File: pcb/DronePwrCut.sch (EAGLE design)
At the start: 55 parts, among them IC1 ATMega48, IC2 MIC5219-3.6YM5-TR, M1 AUIRFS8409-7P, M2 AUIRFS8409-7P, M3 AUIRFS8409-7P, M4 AUIRFS8409-7P, Q1 NF, X1 ISP

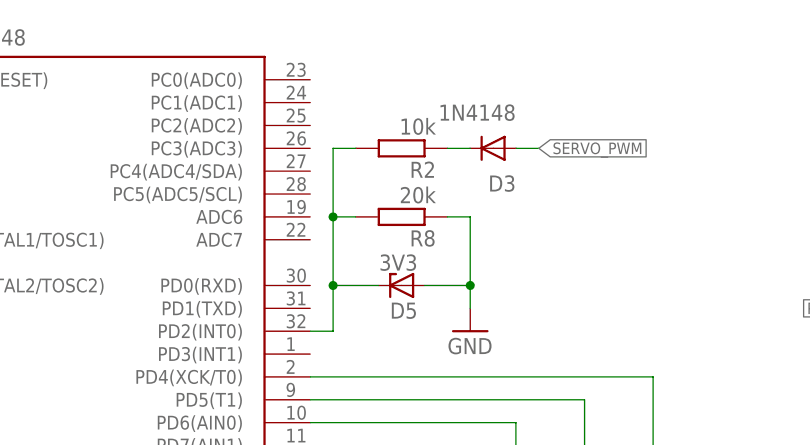
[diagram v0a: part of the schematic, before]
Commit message: Change resistor values (R2, R8) to handle low voltage (3V3) input signals correctly
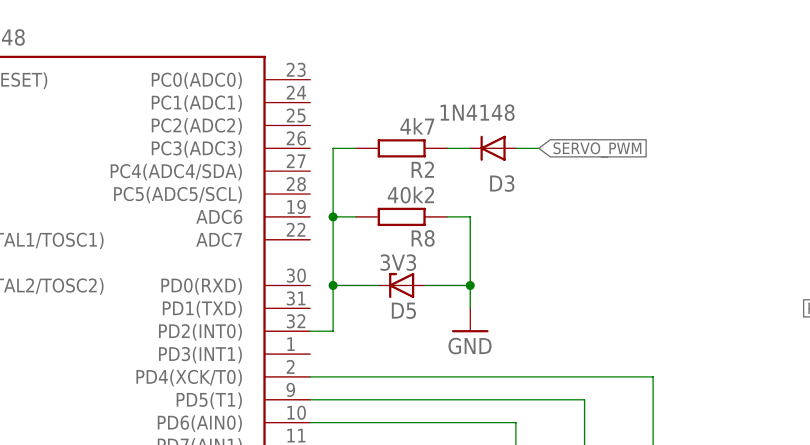
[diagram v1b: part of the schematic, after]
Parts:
- R2: value 10k -> 4k7
- R8: value 20k -> 40k2
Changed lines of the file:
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@@
 <part name="R1" library="rcl" deviceset="R-EU_" device="R1206" value="27k"/>
 <part name="GND7" library="supply1" deviceset="GND" device=""/>
-<part name="R2" library="rcl" deviceset="R-EU_" device="R1206" value="10k"/>
+<part name="R2" library="rcl" deviceset="R-EU_" device="R1206" value="4k7"/>
 <part name="GND8" library="supply1" deviceset="GND" device=""/>
 <part name="R3" library="rcl" deviceset="R-EU_" device="R1206" value="10k"/>
@@
 <part name="PAD1_BAT+" library="wirepad" deviceset="1,6/0,8" device="" value="BAT+"/>
 <part name="PAD1_V-" library="wirepad" deviceset="1,6/0,8" device="" value="V-"/>
-<part name="R8" library="rcl" deviceset="R-EU_" device="R1206" value="20k"/>
+<part name="R8" library="rcl" deviceset="R-EU_" device="R1206" value="40k2"/>
 <part name="PAD3_V-" library="wirepad" deviceset="1,6/0,8" device="" value="V-"/>
 <part name="PAD4_V-" library="wirepad" deviceset="1,6/0,8" device="" value="V-"/>
